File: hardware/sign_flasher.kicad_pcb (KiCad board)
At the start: 2 copper layers, 106.7 x 106.7 mm, 46 parts, among them J1 Battery, Q1 BC557, Q2 BC547, U1 NE555D, U2 NE555D

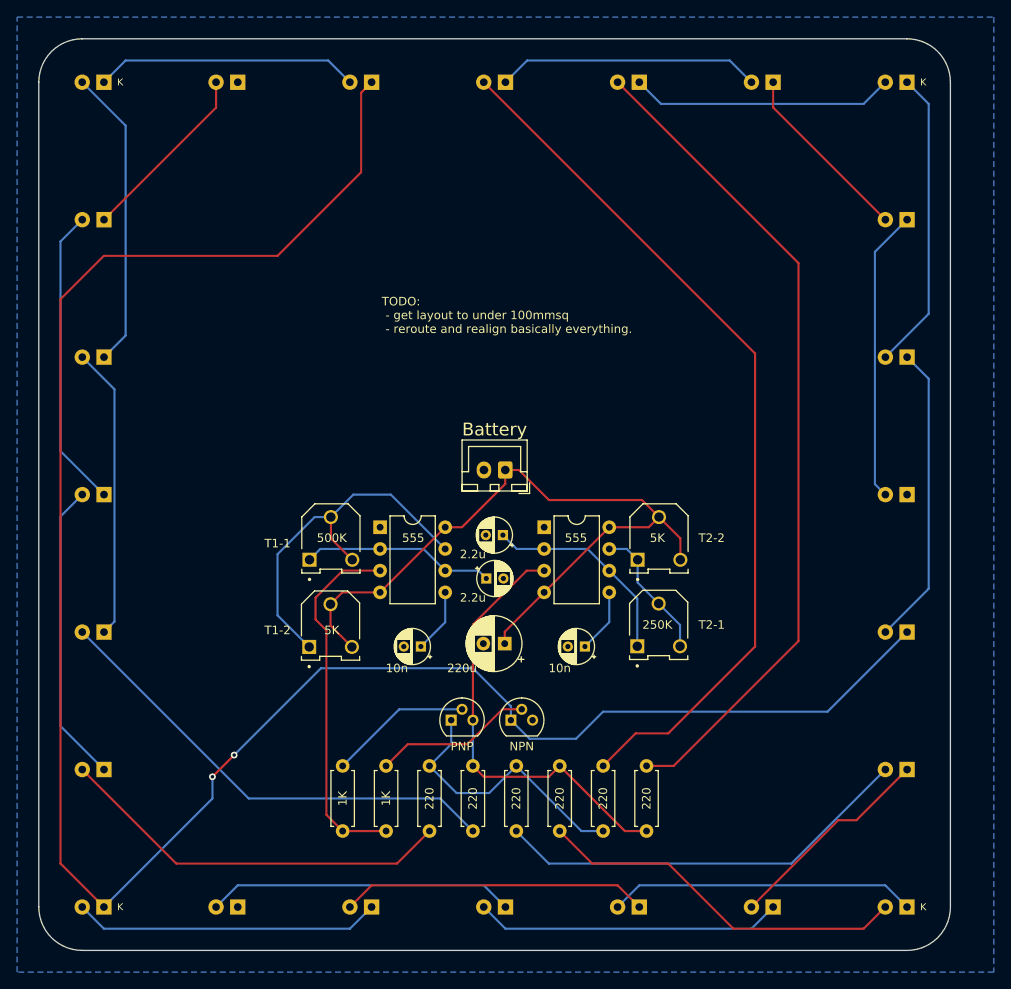
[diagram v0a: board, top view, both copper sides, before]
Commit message: get under 100mmsq, add mounting holes
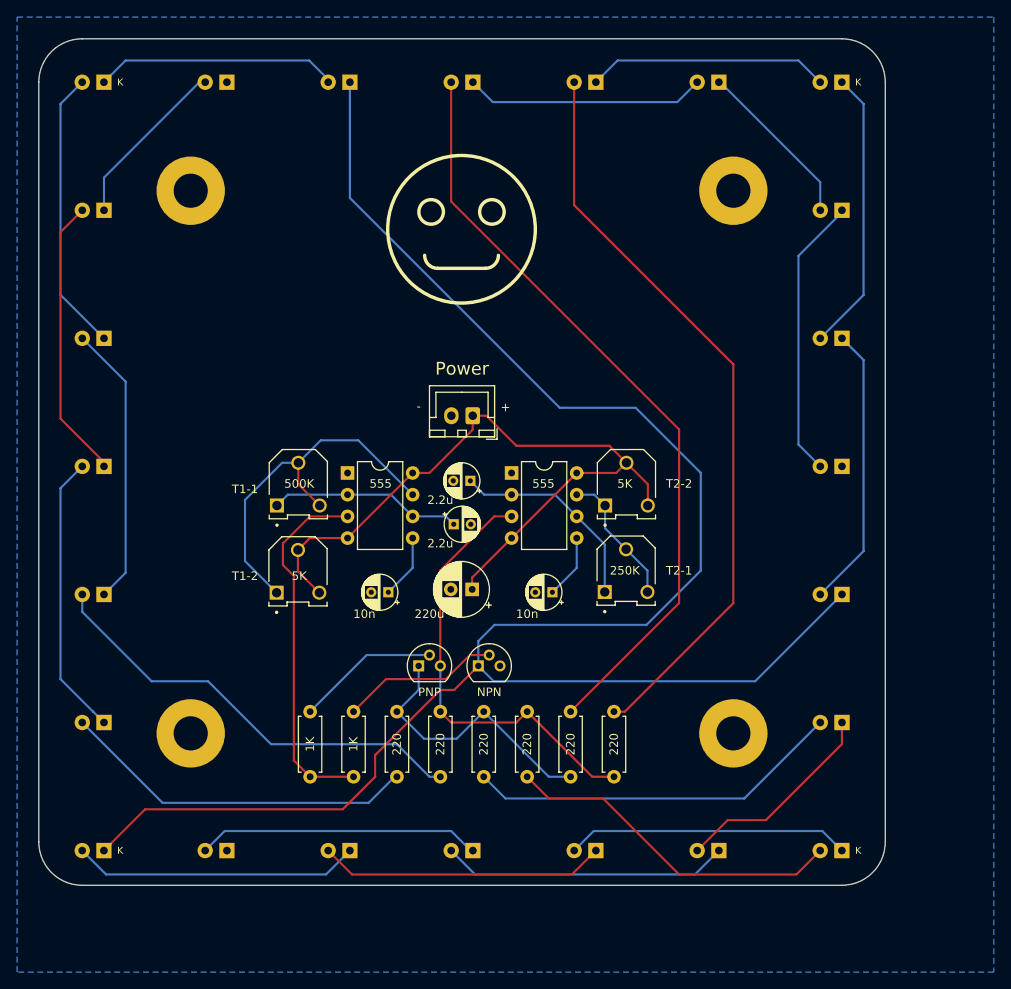
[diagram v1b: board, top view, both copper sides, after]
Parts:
- added H1: MountingHole, MountingHole:MountingHole_4mm_Pad, F.Cu at (165.1, 61.0)
- added H2: MountingHole, MountingHole:MountingHole_4mm_Pad, F.Cu at (101.6, 61.0)
- added H3: MountingHole, MountingHole:MountingHole_4mm_Pad, F.Cu at (165.1, 124.5)
- added H4: MountingHole, MountingHole:MountingHole_4mm_Pad, F.Cu at (101.6, 124.5)
- J1: value Battery -> Power
- moved D21 10.1 mm to (177.8, 138.2)
- moved D9 9.40 mm to (177.8, 123.2)
- moved D10 9.16 mm to (163.4, 138.2)
- moved D20 8.80 mm to (177.8, 108.2)
- moved D22 8.33 mm to (149.0, 138.2)
- moved D8 8.30 mm to (177.8, 93.2)
- moved D19 7.93 mm to (177.8, 78.2)
- moved D7 7.70 mm to (177.8, 63.2)
- moved D11 7.62 mm to (134.6, 138.2)
- moved D18 7.62 mm to (177.8, 48.3)
- moved C2 7.41 mm to (132.4, 100.0)
- moved C4 7.41 mm to (134.3, 94.9)
- moved Q1 7.41 mm to (128.3, 116.6)
- moved Q2 7.41 mm to (135.3, 116.6)
- moved R4 7.41 mm to (135.9, 121.9)
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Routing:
- net Net-(D16-K): track 242.2 -> 213.5 mm, vias 2 -> 0
- net Net-(D5-A): track 102.8 -> 90.0 mm
- net Net-(D17-A): track 98.0 -> 87.9 mm
- net Net-(D9-A): track 49.3 -> 44.1 mm
- net Net-(D1-A): track 46.8 -> 42.0 mm
- net Net-(D21-A): track 43.9 -> 40.2 mm
- net Net-(D13-A): track 55.4 -> 51.9 mm
- net Net-(D11-K): track 36.0 -> 33.2 mm
- net Net-(D21-K): track 36.0 -> 33.2 mm
- net Net-(D5-K): track 30.9 -> 28.2 mm
- net Net-(D17-K): track 30.9 -> 28.4 mm
- net Net-(D15-K): track 30.9 -> 28.5 mm
- net Net-(D22-K): track 36.0 -> 33.6 mm
- net Net-(D23-K): track 36.0 -> 33.6 mm
- net Net-(D10-K): track 36.0 -> 33.6 mm
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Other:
- board size 106.7 x 106.7 mm -> 99.1 x 99.1 mm
- board text removed: "TODO: - get layout to under 100mmsq - reroute and realign basically everything."
